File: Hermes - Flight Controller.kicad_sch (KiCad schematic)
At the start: 28 parts, among them J1 USB_C_Receptacle_USB2.0, J2 Batt1, J3 Batt2, Q1 DMP3013SFV, SW1 SW_SPDT, U1 AP2127K-3.3, U2 USBLC6-2SC6, U3 BQ25887RGER

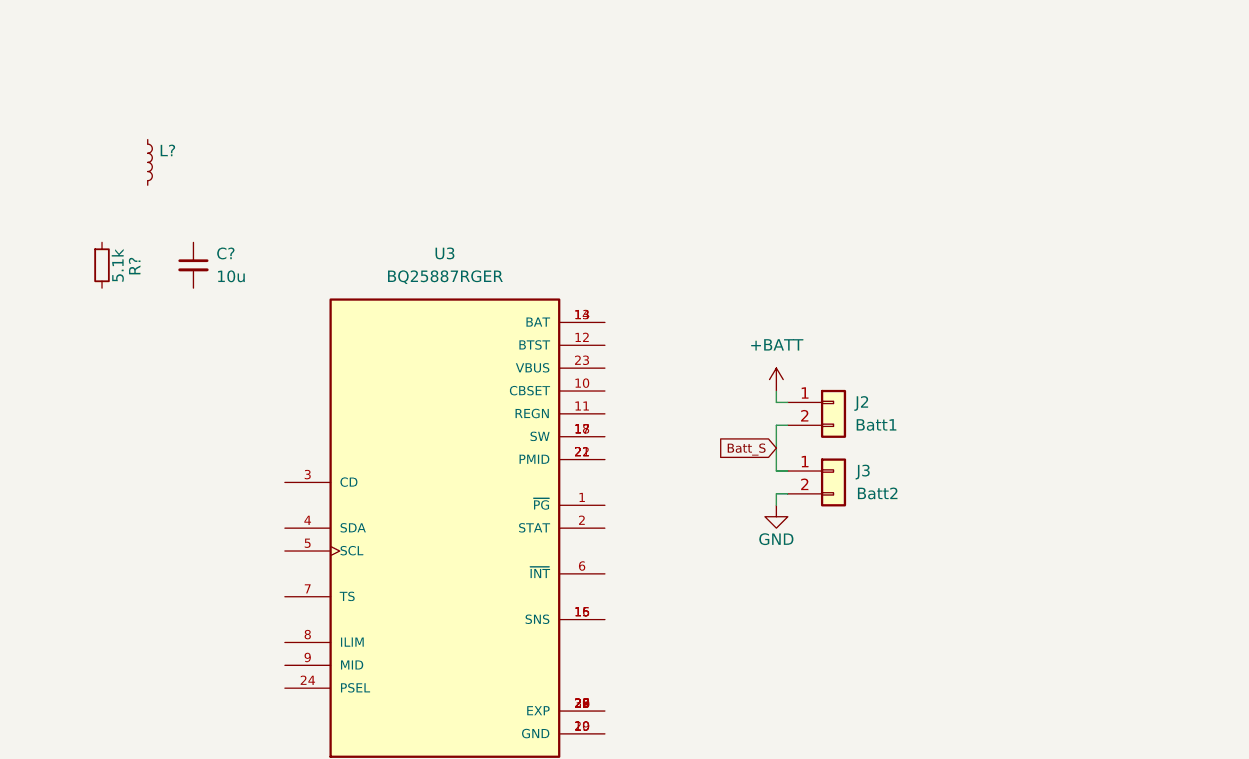
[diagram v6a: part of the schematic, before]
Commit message: 2s2p config -> more powa
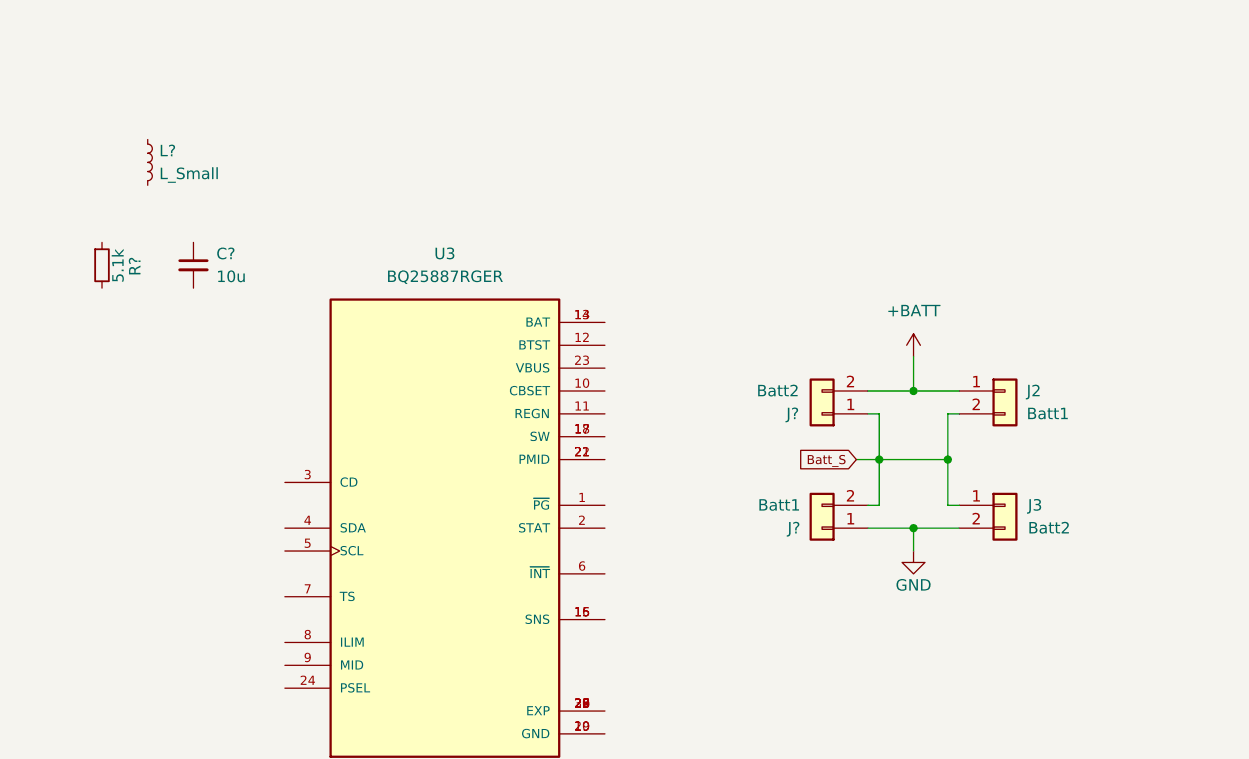
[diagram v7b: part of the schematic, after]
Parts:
- added J?: Batt1, symbol Connector_Generic:Conn_01x02
- added J?: Batt2, symbol Connector_Generic:Conn_01x02
- L?: value (none) -> L_Small
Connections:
- net +BATT: now also J?.2 (Pin_2)
- net Batt_S: now also J?.1 (Pin_1), J?.2 (Pin_2)
- net GND: now also J?.1 (Pin_1)
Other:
- moved on the sheet: J2, J3

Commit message: rp2040
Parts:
- gave numbers to parts that had none: 5
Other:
- added sheet MCU (MCU.kicad_sch)
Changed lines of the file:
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@@
   (symbol (lib_id "Device:R_Small") (at 25.4 121.92 0) (unit 1)
     (in_bom yes) (on_board yes)
-    (property "Reference" "R?" (id 0) (at 29.0846 122.0355 90))
+    (property "Reference" "R7" (id 0) (at 29.0846 122.0355 90))
     (property "Value" "5.1k" (id 1) (at 27.2155 121.985 90))
     (property "Footprint" "Resistor_SMD:R_0603_1608Metric_Pad0.98x0.95mm_HandSolder" (id 2) (at 25.4 121.92 0)
@@
   (symbol (lib_id "power:GND") (at 115.57 153.67 0) (unit 1)
     (in_bom yes) (on_board yes)
-    (property "Reference" "#PWR?" (id 0) (at 115.57 160.02 0)
+    (property "Reference" "#PWR0104" (id 0) (at 115.57 160.02 0)
       (effects (font (size 1.27 1.27)) hide)
     )
@@
   (symbol (lib_id "Connector_Generic:Conn_01x02") (at 105.41 151.13 180) (unit 1)
     (in_bom yes) (on_board yes) (fields_autoplaced)
-    (property "Reference" "J?" (id 0) (at 103.0071 151.1301 0)
+    (property "Reference" "J5" (id 0) (at 103.0071 151.1301 0)
       (effects (font (size 1.27 1.27)) (justify left))
     )
@@
   (symbol (lib_id "Connector_Generic:Conn_01x02") (at 105.41 138.43 180) (unit 1)
     (in_bom yes) (on_board yes) (fields_autoplaced)
-    (property "Reference" "J?" (id 0) (at 102.87 138.4301 0)
+    (property "Reference" "J4" (id 0) (at 102.87 138.4301 0)
       (effects (font (size 1.27 1.27)) (justify left))
     )
@@
   (symbol (lib_id "Device:L_Small") (at 30.48 110.49 0) (unit 1)
     (in_bom yes) (on_board yes) (fields_autoplaced)
-    (property "Reference" "L?" (id 0) (at 31.75 109.2199 0)
+    (property "Reference" "L1" (id 0) (at 31.75 109.2199 0)
       (effects (font (size 1.27 1.27)) (justify left))
     )
@@
   (symbol (lib_id "Device:C_Small") (at 35.56 121.92 0) (unit 1)
     (in_bom yes) (on_board yes) (fields_autoplaced)
-    (property "Reference" "C?" (id 0) (at 38.1 120.6562 0)
+    (property "Reference" "C9" (id 0) (at 38.1 120.6562 0)
       (effects (font (size 1.27 1.27)) (justify left))
     )
@@
     (pin "2")
   )
+  (sheet (at 237.49 134.62) (size 7.62 6.35) (fields_autoplaced)
+    (stroke (width 0.1524) (type solid) (color 0 0 0 0))
+    (fill (color 0 0 0 0.0000))
+    (property "Sheet name" "MCU" (id 0) (at 237.49 133.9084 0)
+      (effects (font (size 1.27 1.27)) (justify left bottom))
+    )
+    (property "Sheet file" "MCU.kicad_sch" (id 1) (at 237.49 141.5546 0)
+      (effects (font (size 1.27 1.27)) (justify left top))
+    )
+  )
   (sheet_instances
     (path "/" (page "1"))
+    (path "/cf1c0b30-e009-423a-8a61-24e0288be5ef" (page "2"))
   )
   (symbol_instances
@@
       (reference "#PWR0103") (unit 1) (value "GND") (footprint "")
     )
+    (path "/5c514e44-33e2-4c4b-ae7f-50636654683c"
+      (reference "#PWR0104") (unit 1) (value "GND") (footprint "")
+    )
     (path "/124c0897-d684-4385-816d-75ab5df8cfd8"
       (reference "#PWR0105") (unit 1) (value "+3.3V") (footprint "")
@@
       (reference "#PWR0122") (unit 1) (value "GND") (footprint "")
     )
-    (path "/5c514e44-33e2-4c4b-ae7f-50636654683c"
-      (reference "#PWR?") (unit 1) (value "GND") (footprint "")
-    )
     (path "/5d908da2-6c54-41bb-9c7b-ab3775858c1d"
       (reference "C1") (unit 1) (value "100u") (footprint "Resistor_SMD:R_0805_2012Metric_Pad1.20x1.40mm_HandSolder")
@@
     )
     (path "/b7ae69ff-1864-495f-8d8f-fcbb2d70fbdb"
-      (reference "C?") (unit 1) (value "10u") (footprint "Capacitor_SMD:C_0603_1608Metric_Pad1.08x0.95mm_HandSolder")
+      (reference "C9") (unit 1) (value "10u") (footprint "Capacitor_SMD:C_0603_1608Metric_Pad1.08x0.95mm_HandSolder")
     )
     (path "/f7d44a9f-c08a-4bcb-8cd3-fc8f62a6b9a1"
@@
       (reference "J3") (unit 1) (value "Batt2") (footprint "")
     )
+    (path "/aec76fa7-ca3b-4002-827b-890c008964e6"
+      (reference "J4") (unit 1) (value "Batt2") (footprint "")
+    )
     (path "/a6da1c49-f5f8-4bd8-8a1f-6e9f0765716a"
-      (reference "J?") (unit 1) (value "Batt1") (footprint "")
-    )
-    (path "/aec76fa7-ca3b-4002-827b-890c008964e6"
-      (reference "J?") (unit 1) (value "Batt2") (footprint "")
+      (reference "J5") (unit 1) (value "Batt1") (footprint "")
     )
     (path "/b70e6905-3e7f-42b5-b603-6801221c199d"
-      (reference "L?") (unit 1) (value "L_Small") (footprint "")
+      (reference "L1") (unit 1) (value "L_Small") (footprint "")
     )
     (path "/d35736f0-de68-454d-9fb0-1a81541e123d"
@@
     )
     (path "/4d52a372-9420-451c-af50-8f5f380e48e0"
-      (reference "R?") (unit 1) (value "5.1k") (footprint "Resistor_SMD:R_0603_1608Metric_Pad0.98x0.95mm_HandSolder")
+      (reference "R7") (unit 1) (value "5.1k") (footprint "Resistor_SMD:R_0603_1608Metric_Pad0.98x0.95mm_HandSolder")
     )
     (path "/4b2d920c-152a-4ef8-af7a-b811aec6cc05"
@@
       (reference "U3") (unit 1) (value "BQ25887RGER") (footprint "SnapEDA Library:IC_BQ25887RGER")
     )
-  )
+    (path "/cf1c0b30-e009-423a-8a61-24e0288be5ef/e8e1f712-0deb-4f67-83d0-c85b4f0b9245"
+      (reference "U4") (unit 1) (value "RP2040") (footprint "IC57_RP2040")
+    )
+  )
